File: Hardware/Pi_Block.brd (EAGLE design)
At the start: 30.5 x 87.6 mm, 47 parts, among them U1 PCA9306, U2 EDISON_CONNECTOR_FULLMOUNTING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, U3 EDISON_CONNECTOR_FULLHEADER, U4 TPS62065, U5 MIC5219 3.3V

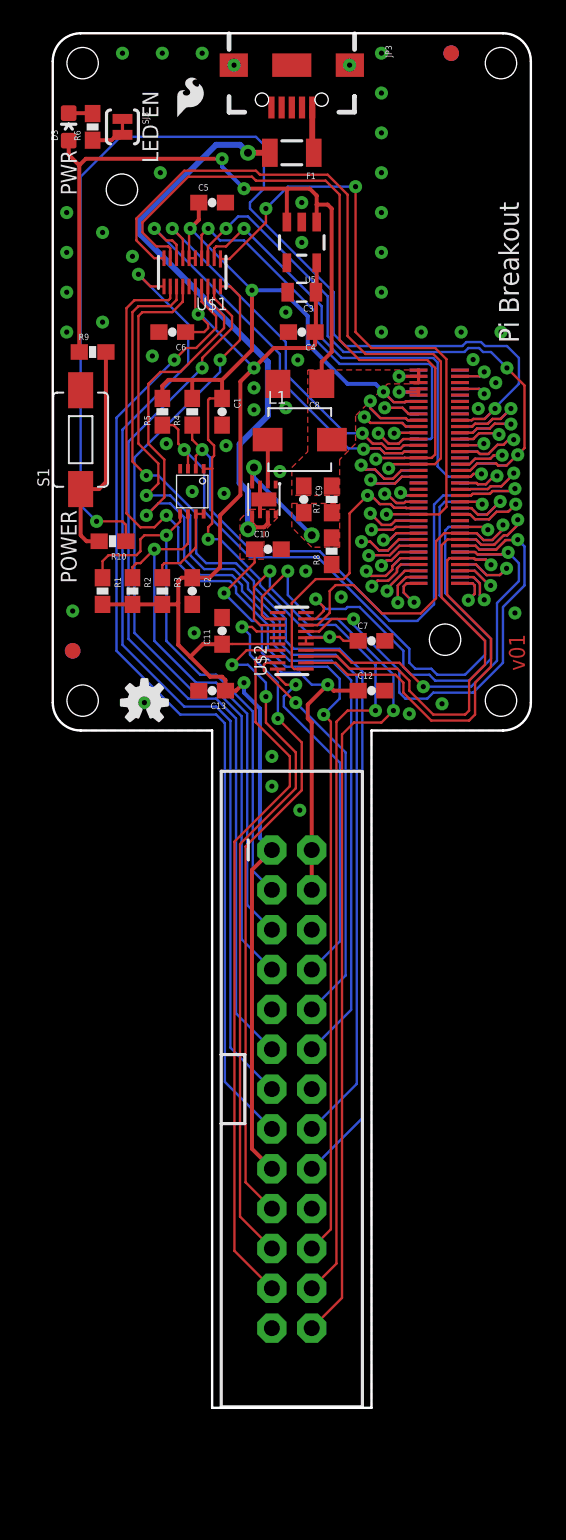
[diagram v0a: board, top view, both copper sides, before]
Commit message: Replaced Header footprint Included DCIN pin Renamed boards Renamed files Replaces power button with side shooting SMD Cleaned up dimensions
TODO: solve power situation between VSYS and DCIN
TODO: Add pass through via for DCIN
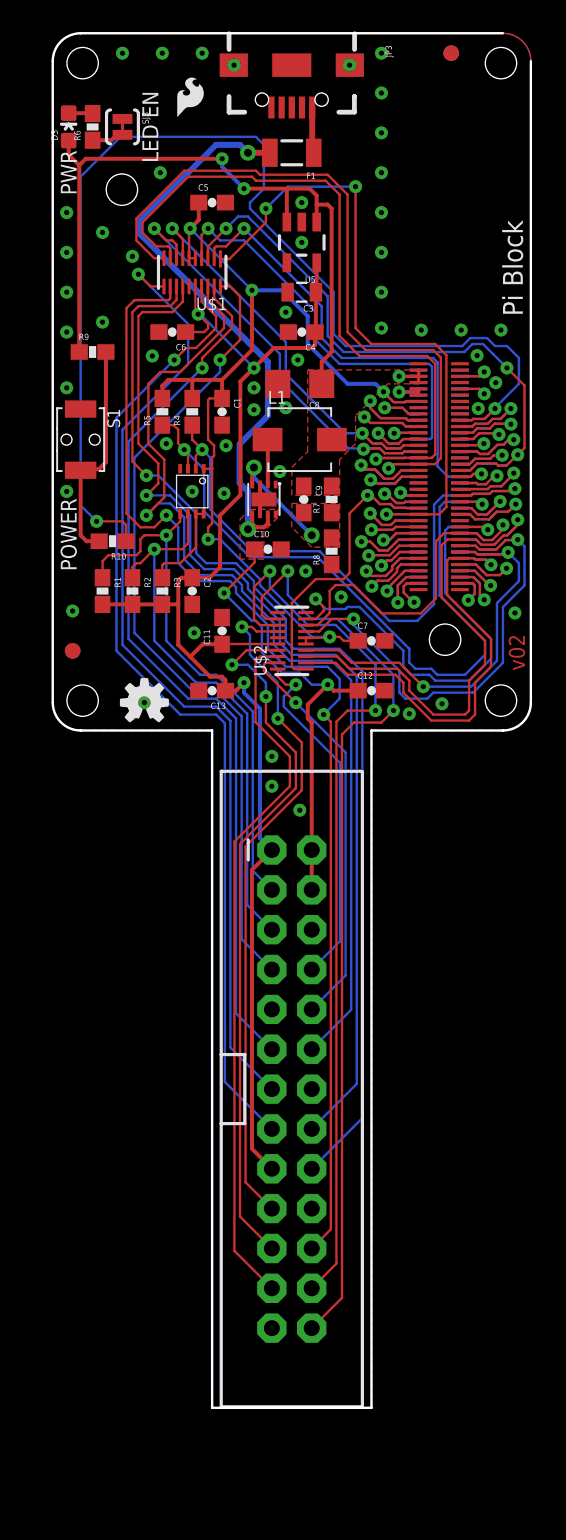
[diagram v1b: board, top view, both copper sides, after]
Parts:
- S1: device SparkFun-Electromechanical:TACTILE-SWITCH-1101NE -> SparkFun-Electromechanical:TACTILE_SWITCH-SMD-RIGHT-ANGLE
- turned S1 to 270 degrees
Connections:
- new net DCIN: U2.14, U3.14
- net GND: now also S1.1; no longer S1.P$2
- net N$15: now also S1.2; no longer S1.P$1
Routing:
- net GND: vias 51 -> 53
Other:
- board text added: "Pi Block"
- board text added: "v02"
- board text removed: "Connectors Go Here"
- board text removed: "LED's and selector switches go here"
- board text removed: "Max Board Length"
- board text removed: "Nothing goes here... I mean it."
- board text removed: "Pi Breakout"
- board text removed: "v01"

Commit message: Added Vsys-to-5V diode. Added DCIN to Vsys MOSFET. Added slants to board dimension near Pi connector for stability.
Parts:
- added D1: BAT20J, SparkFun-DiscreteSemi:SOD-323
- added Q1: BSS138, SparkFun-DiscreteSemi:SOT23-3
- added R11: 1K, SparkFun-Resistors:0603-RES
- added SJ1: JUMPER-PAD-2-NOYES_SILK, SparkFun-Passives:PAD-JUMPER-2-NO_YES_SILK
- moved LOGO3 40.4 mm to (25.9, 2.67)
- moved LOGO1 2.84 mm to (4.57, 4.32)
- moved R9 1.02 mm to (2.54, 23.1)
- moved R6 0.25 mm to (2.54, 38.7)
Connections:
- new net N$16: Q1.1, R11.1
- new net N$3: D1.C, SJ1.2
- net 5V: now also R11.2, SJ1.1
- net DCIN: now also Q1.2
- net VSYS: now also D1.A, Q1.3
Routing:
- net DCIN: track 0.00 -> 40.8 mm, vias 0 -> 2
- net 5V: track 66.3 -> 86.8 mm, vias 4 -> 5
- net USB_DP: track 4.65 -> 9.24 mm
- net N$3: track 0.00 -> 3.54 mm
- net USB_DN: track 7.70 -> 10.2 mm
- net VSYS: track 51.2 -> 53.5 mm
- net N$16: track 0.00 -> 1.85 mm
- net PWRBTN#: track 74.8 -> 73.0 mm
- net GP13_PWM1: track 41.1 -> 39.3 mm
- net GP45: track 29.0 -> 30.6 mm
- net 1.8V: track 65.7 -> 67.2 mm
- net GP14: track 42.3 -> 41.0 mm
- net GP48: track 46.4 -> 45.1 mm
- net GP47: track 46.0 -> 44.7 mm
- net N$12: track 1.54 -> 2.76 mm
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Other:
- outline, holes or cut-outs redrawn
- board text added: "VSYS EN"

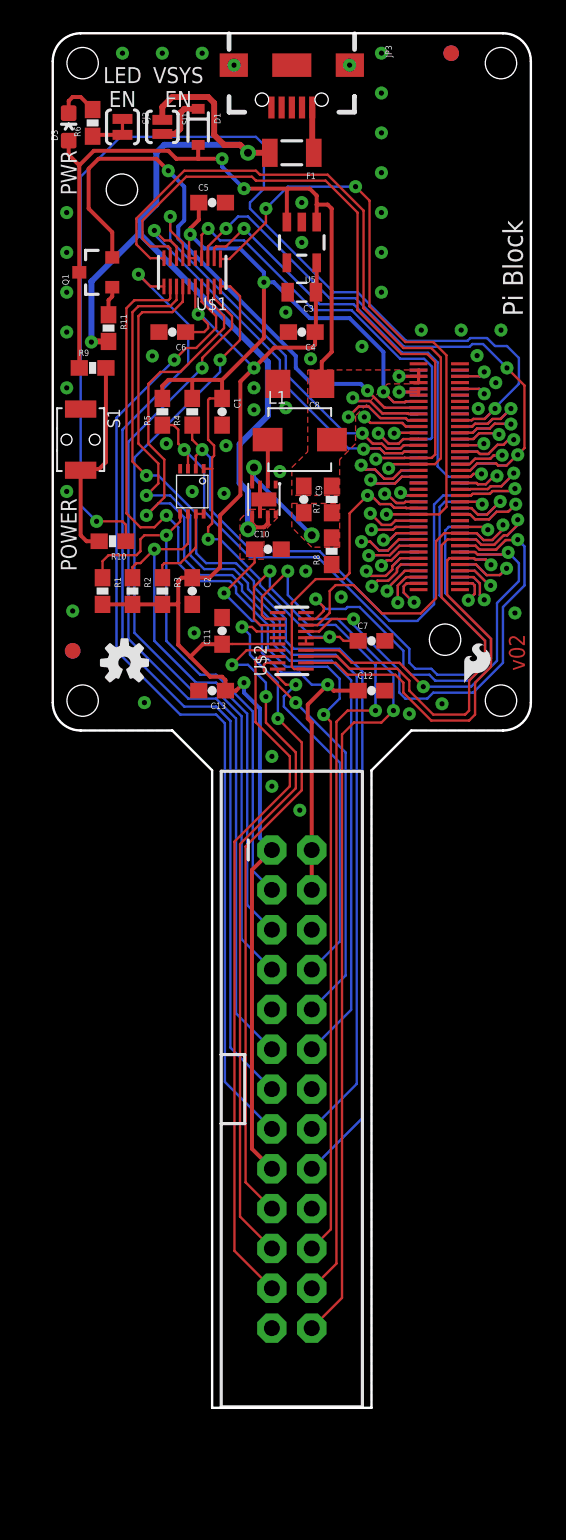
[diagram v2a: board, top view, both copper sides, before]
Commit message: Made R4 and R5 DNP. Added I2C PU solder jumper. Changed I2C PUs to 10k.
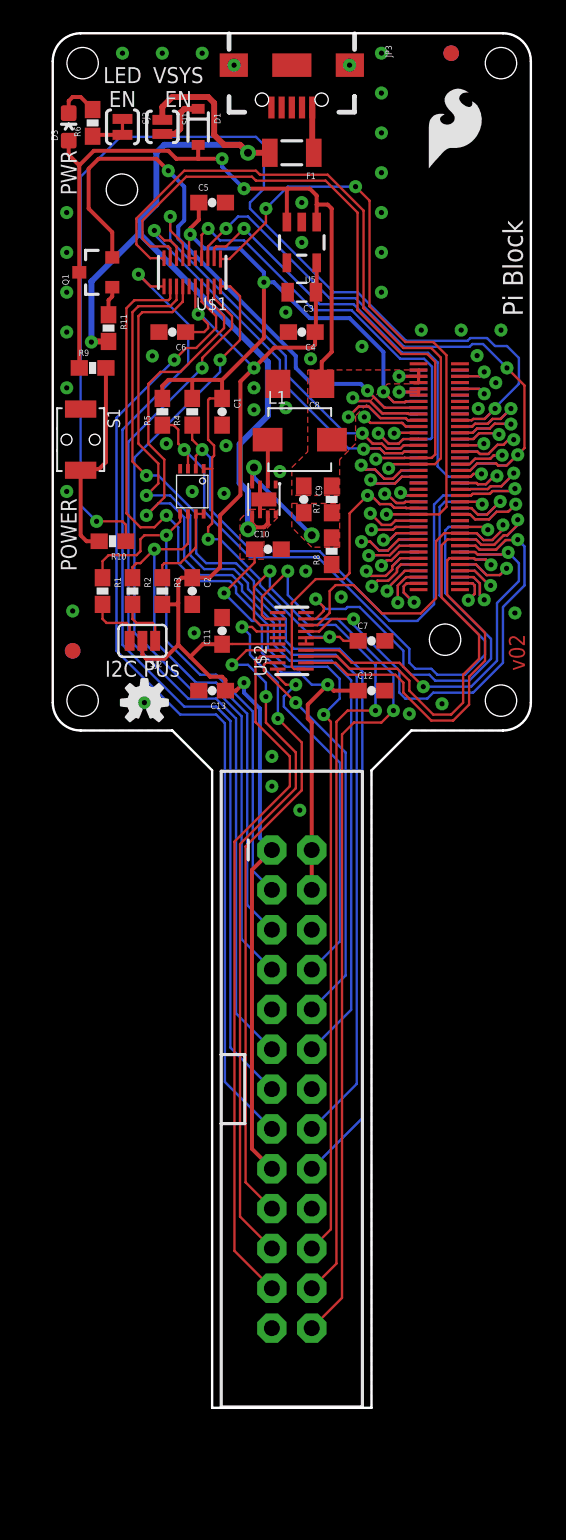
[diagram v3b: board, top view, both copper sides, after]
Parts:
- added SJ2: JUMPER-PAD-3-NC_BY_PASTE, SparkFun-Passives:PAD-JUMPER-3-NC_BY_PASTE_YES_SILK_FULL_BOX
- LOGO3: value SFE_LOGO_FLAME.1_INCH -> SFE_LOGO_FLAME.2_INCH; device SparkFun-Aesthetics:SFE_LOGO_FLAME_.1 -> SparkFun-Aesthetics:SFE_LOGO_FLAME_.2
- R1, R2: value 2.2k -> 10k
- R4, R5: value 2.2k -> DNP
- moved LOGO3 33.0 mm to (23.6, 35.6)
- moved LOGO1 2.84 mm to (5.84, 1.78)
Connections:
- new net N$4: R1.2, SJ2.3
- new net N$5: R2.2, SJ2.1
- net 3.3V_LOCAL: now also SJ2.2; no longer R1.2, R2.2
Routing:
- net N$4: track 0.00 -> 3.78 mm
- net N$5: track 0.00 -> 3.52 mm
- net GP130_UART_1_RX: track 29.4 -> 28.5 mm
- net GP109_SPI_2_CLK: track 35.2 -> 34.4 mm
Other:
- board text added: "I2C PUs"

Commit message: Changed value from 10k to 10K to align with library
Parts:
- R1, R2: value 10k -> 10K
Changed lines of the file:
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@@
 <attribute name="DIST_ID" value="PRT-11490" x="15.24" y="-22.86" size="1.778" layer="27" font="vector" ratio="15" display="off"/>
 </element>
-<element name="R1" library="SparkFun-Resistors" package="0603-RES" value="10k" x="3.175" y="8.89" rot="R270">
+<element name="R1" library="SparkFun-Resistors" package="0603-RES" value="10K" x="3.175" y="8.89" rot="R270">
 <attribute name="PROD_ID" value="RES-00824" x="15.875" y="8.89" size="1.778" layer="27" font="vector" ratio="15" rot="R270" display="off"/>
 </element>
-<element name="R2" library="SparkFun-Resistors" package="0603-RES" value="10k" x="5.08" y="8.89" rot="R270">
+<element name="R2" library="SparkFun-Resistors" package="0603-RES" value="10K" x="5.08" y="8.89" rot="R270">
 <attribute name="PROD_ID" value="RES-00824" x="12.7" y="13.97" size="1.778" layer="27" font="vector" ratio="15" rot="R270" display="off"/>
 </element>

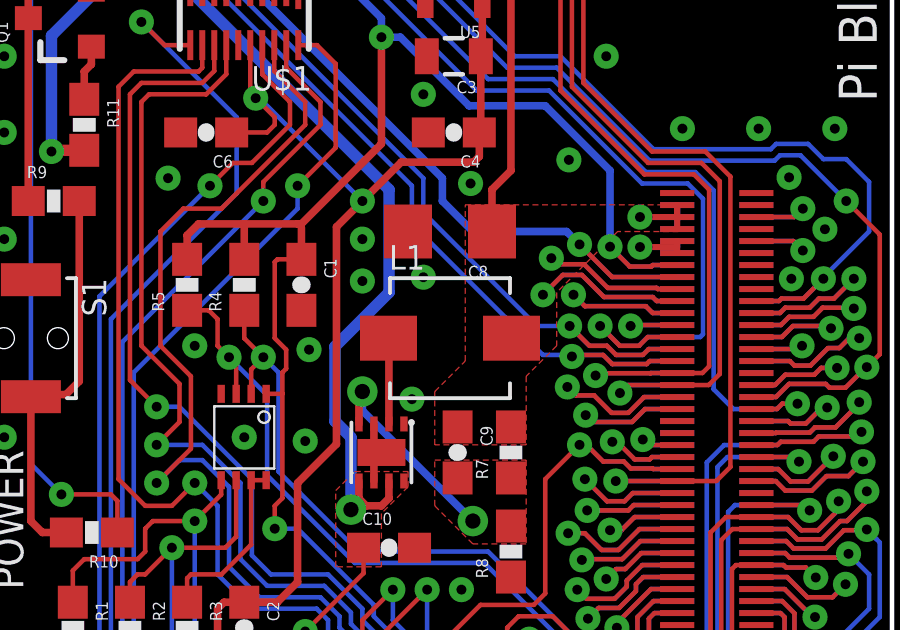
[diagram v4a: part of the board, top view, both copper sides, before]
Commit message: Changed DC/DC output cap to 22uF. Added value to inductor.
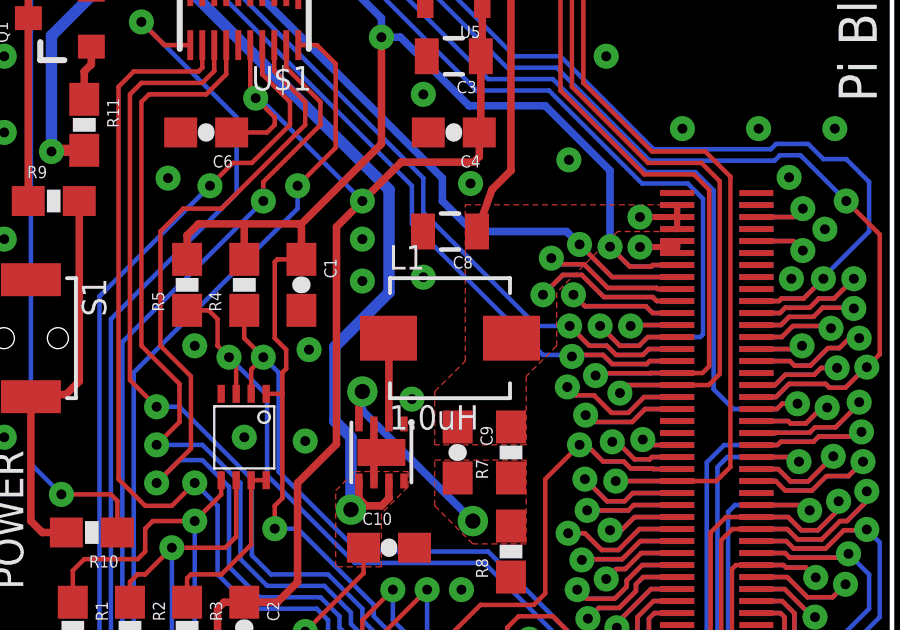
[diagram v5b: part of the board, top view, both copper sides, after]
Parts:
- C8: value 10uF -> 22uF; device SparkFun-Capacitors:1206 -> SparkFun-Capacitors:0805
- L1: value (none) -> 1.0uH
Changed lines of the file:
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@@
 <layer number="2" name="Route2" color="1" fill="3" visible="no" active="yes"/>
 <layer number="15" name="Route15" color="4" fill="6" visible="no" active="yes"/>
-<layer number="16" name="Bottom" color="1" fill="1" visible="yes" active="yes"/>
+<layer number="16" name="Bottom" color="1" fill="1" visible="no" active="yes"/>
 <layer number="17" name="Pads" color="2" fill="1" visible="yes" active="yes"/>
 <layer number="18" name="Vias" color="2" fill="1" visible="yes" active="yes"/>
@@
 <layer number="20" name="Dimension" color="15" fill="1" visible="yes" active="yes"/>
 <layer number="21" name="tPlace" color="16" fill="1" visible="yes" active="yes"/>
-<layer number="22" name="bPlace" color="14" fill="1" visible="yes" active="yes"/>
+<layer number="22" name="bPlace" color="14" fill="1" visible="no" active="yes"/>
 <layer number="23" name="tOrigins" color="15" fill="1" visible="yes" active="yes"/>
-<layer number="24" name="bOrigins" color="15" fill="1" visible="yes" active="yes"/>
+<layer number="24" name="bOrigins" color="15" fill="1" visible="no" active="yes"/>
 <layer number="25" name="tNames" color="7" fill="1" visible="no" active="yes"/>
 <layer number="26" name="bNames" color="7" fill="1" visible="no" active="yes"/>
@@
 <layer number="43" name="vRestrict" color="2" fill="10" visible="no" active="yes"/>
 <layer number="44" name="Drills" color="7" fill="1" visible="no" active="yes"/>
-<layer number="45" name="Holes" color="7" fill="1" visible="yes" active="yes"/>
+<layer number="45" name="Holes" color="7" fill="1" visible="no" active="yes"/>
 <layer number="46" name="Milling" color="3" fill="1" visible="no" active="yes"/>
-<layer number="51" name="tDocu" color="6" fill="1" visible="yes" active="yes"/>
+<layer number="51" name="tDocu" color="6" fill="1" visible="no" active="yes"/>
 <layer number="52" name="bDocu" color="7" fill="1" visible="no" active="yes"/>
 <layer number="3" name="Route3" color="4" fill="3" visible="no" active="no"/>
@@
 </element>
 <element name="SJ3" library="SparkFun-Passives" package="PAD-JUMPER-2-NC_BY_TRACE_YES_SILK" value="JUMPER-PAD-2-NC_BY_TRACE" x="4.445" y="38.481" rot="R270"/>
-<element name="C8" library="SparkFun-Capacitors" package="1206" value="10uF" x="15.748" y="22.098" rot="R180">
-<attribute name="PROD_ID" value="CAP-10057" x="25.908" y="14.478" size="1.778" layer="27" font="vector" ratio="15" rot="R180" display="off"/>
+<element name="C8" library="SparkFun-Capacitors" package="0805" value="22uF" x="15.748" y="22.098" rot="R180">
+<attribute name="PROD_ID" value="CAP-08402" x="25.908" y="14.478" size="1.778" layer="27" font="vector" ratio="15" rot="R180" display="off"/>
 </element>
 <element name="U4" library="Testing" package="WSON-8-PAD" value="TPS62065" x="13.462" y="14.732" rot="R180"/>
@@
 <attribute name="PROD_ID" value="CAP-08280" x="-1.524" y="3.937" size="1.778" layer="27" font="vector" ratio="15" display="off"/>
 </element>
-<element name="L1" library="SparkFun-Passives" package="INDUCTOR-SRP4020" value="" x="15.748" y="18.542"/>
+<element name="L1" library="SparkFun-Passives" package="INDUCTOR-SRP4020" value="1.0uH" x="15.748" y="18.542">
+<attribute name="PROD_ID" value="NDUC-12274" x="15.748" y="18.542" size="1.778" layer="27" display="off"/>
+</element>
 <element name="U$1" library="Testing" package="UFDFN-20" value="TXB0108" x="8.89" y="29.21" rot="R180"/>
 <element name="U$2" library="Testing" package="UFDFN-20" value="TXB0108" x="15.24" y="5.715" rot="R90"/>
@@
 <vertex x="16.256" y="17.78"/>
 </polygon>
-<wire x1="17.148" y1="22.098" x2="17.148" y2="23.498" width="0.254" layer="1"/>
+<wire x1="16.648" y1="22.098" x2="17.148" y2="23.498" width="0.254" layer="1"/>
 <wire x1="17.148" y1="23.498" x2="17.78" y2="24.13" width="0.254" layer="1"/>
 <wire x1="17.78" y1="24.13" x2="17.78" y2="33.274" width="0.254" layer="1"/>

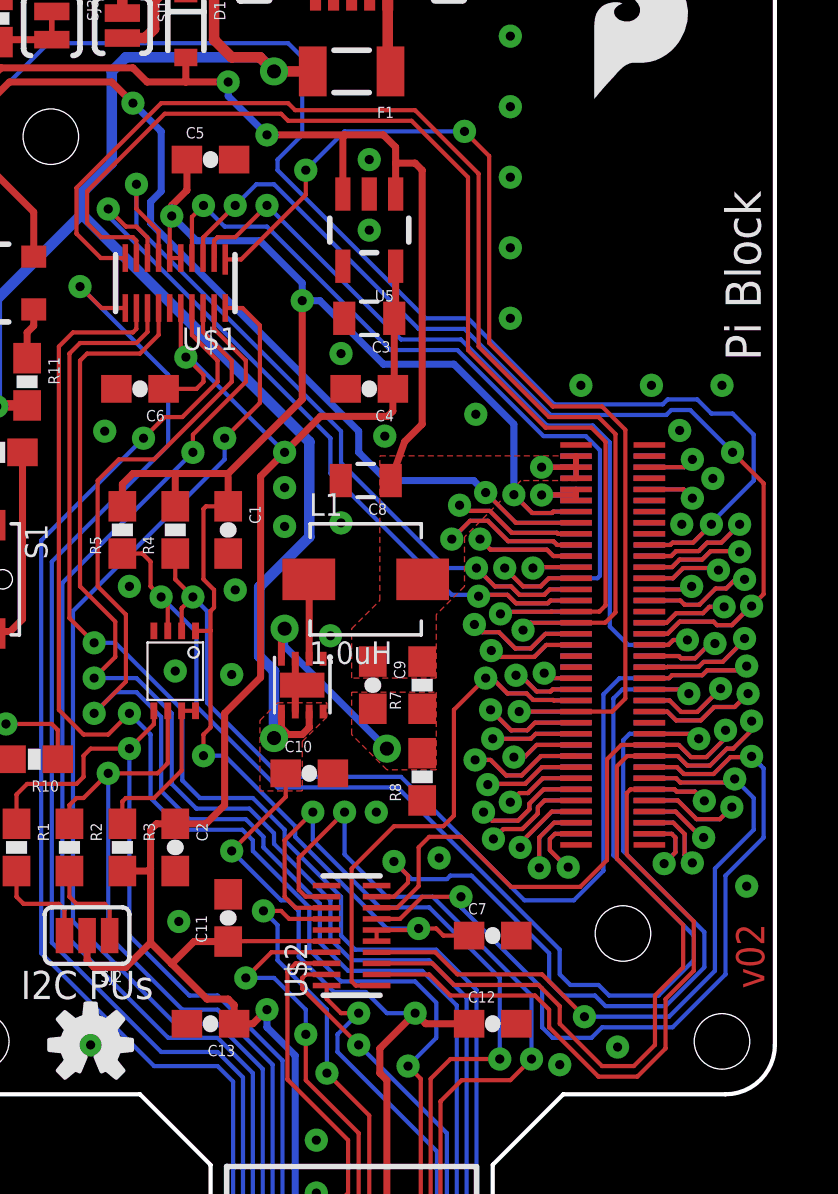
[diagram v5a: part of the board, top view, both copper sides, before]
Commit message: Added silk to Pi pins. Moved a few traces to straighten them or prevent bridging of pins.
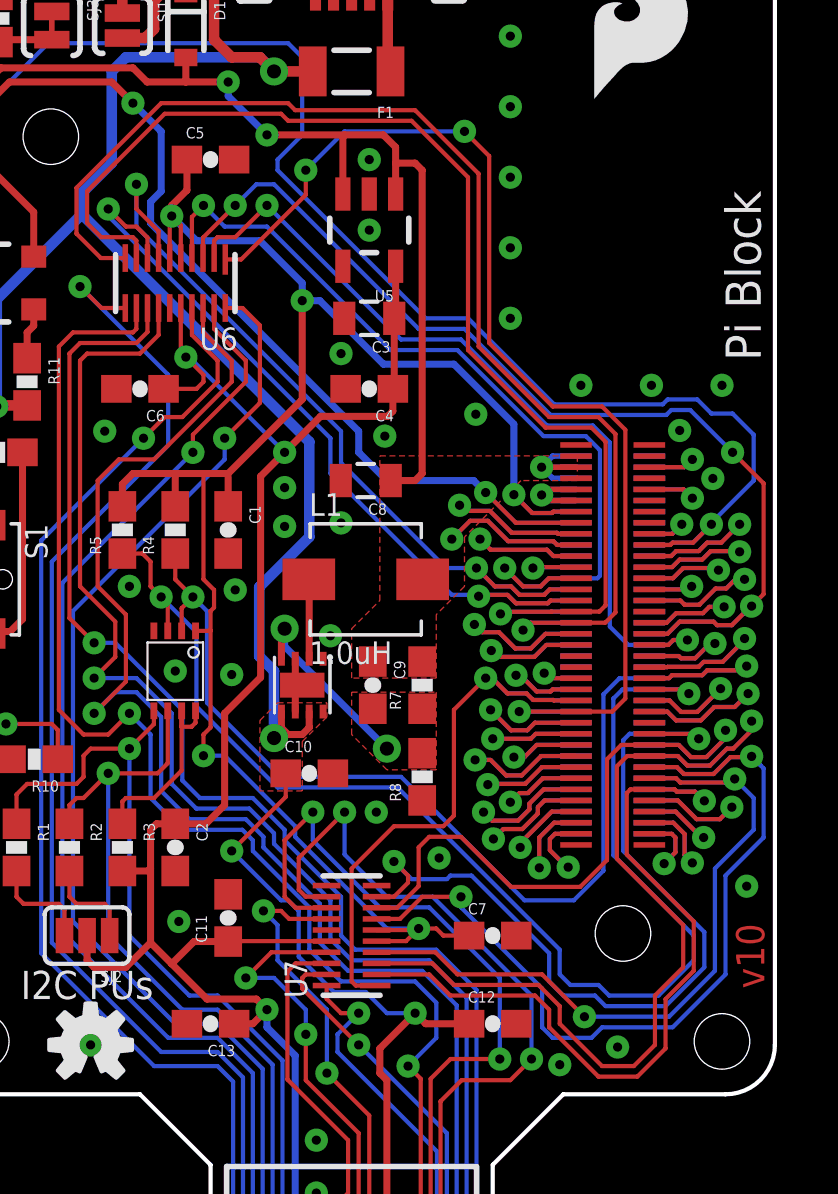
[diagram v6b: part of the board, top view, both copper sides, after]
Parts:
- renumbered U$1 to U6, U$2 to U7
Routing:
- net 1.8V: track 67.2 -> 70.1 mm
- net GND: track 2.11 -> 4.73 mm
- net 3.3V: track 3.68 -> 5.29 mm
- net VSYS: track 53.6 -> 55.0 mm
- net N$1: track 6.05 -> 7.12 mm
- net 3.3V_LOCAL: track 89.4 -> 90.0 mm
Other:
- board text added: "3.3V"
- board text added: "5V"
- board text added: "CE0"
- board text added: "CE1"
- board text added: "G17"
- board text added: "G18"
- board text added: "G22"
- board text added: "G23"
- board text added: "G24"
- board text added: "G25"
- board text added: "G27"
- board text added: "G4"
- board text added: "GND"
- board text added: "MISO"
- board text added: "MOSI"
- board text added: "RXI"
- board text added: "SCK"
- board text added: "SCL"
- board text added: "SDA"
- board text added: "TXO"
- board text added: "v10"
- board text removed: "v02"
